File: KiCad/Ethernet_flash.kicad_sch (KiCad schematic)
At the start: 45 parts, among them IC10 TS3DV642A0RUAR, IC11 LSF0204GU12, IC8 TFP410PAP, IC9 MX25UM25645GXDI00-T

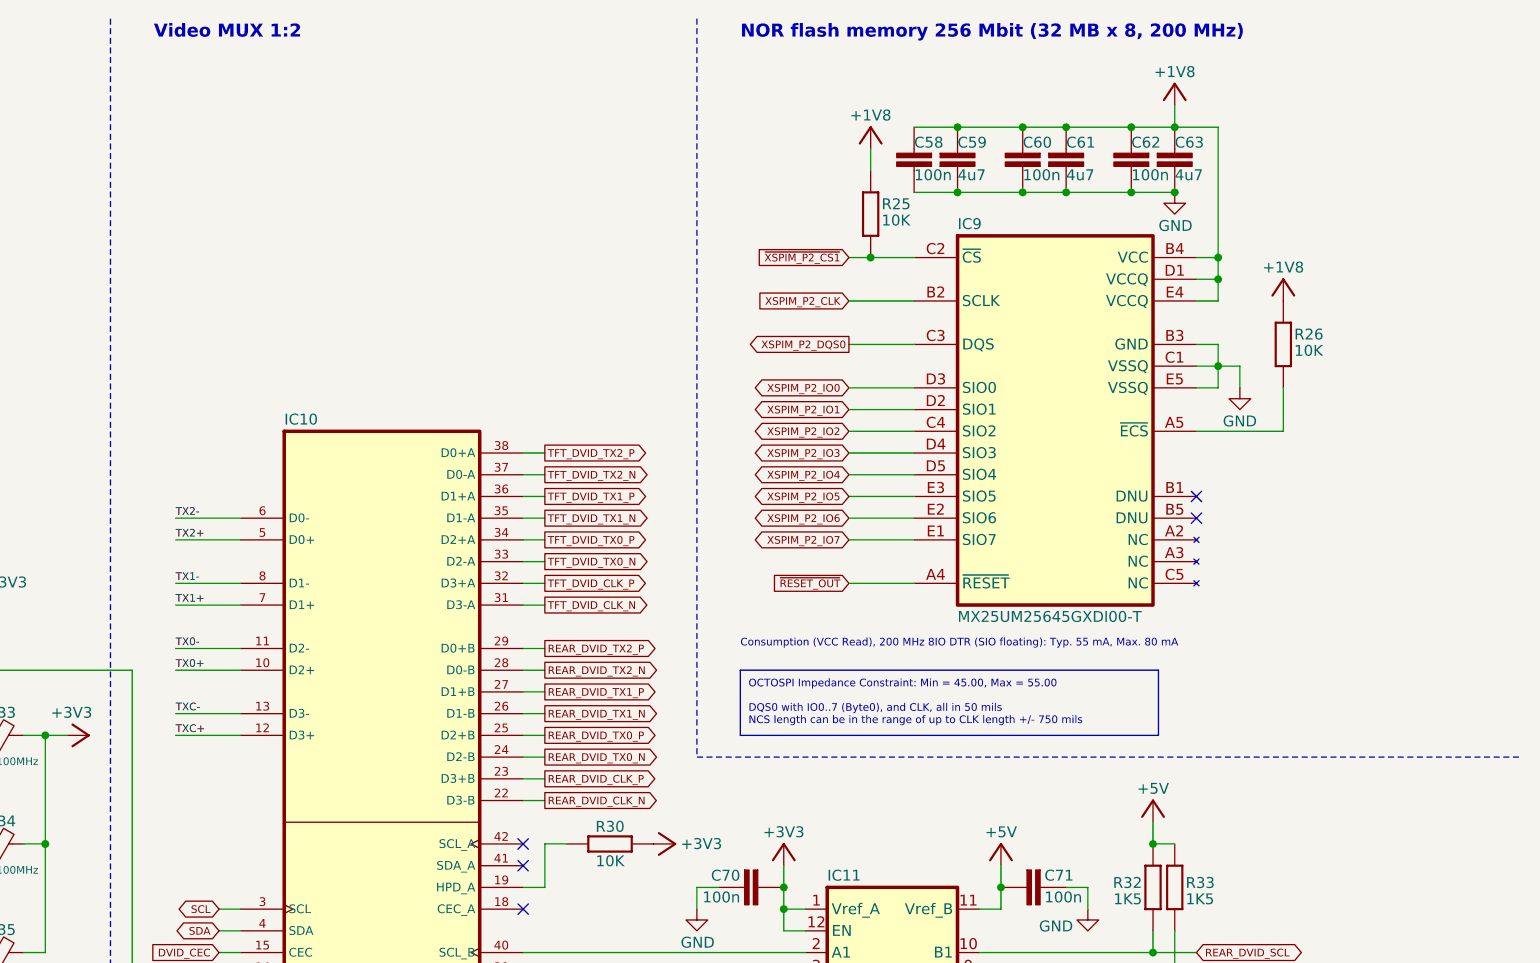
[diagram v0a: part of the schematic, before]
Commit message: USB lanes renamed, OSHWA logo added
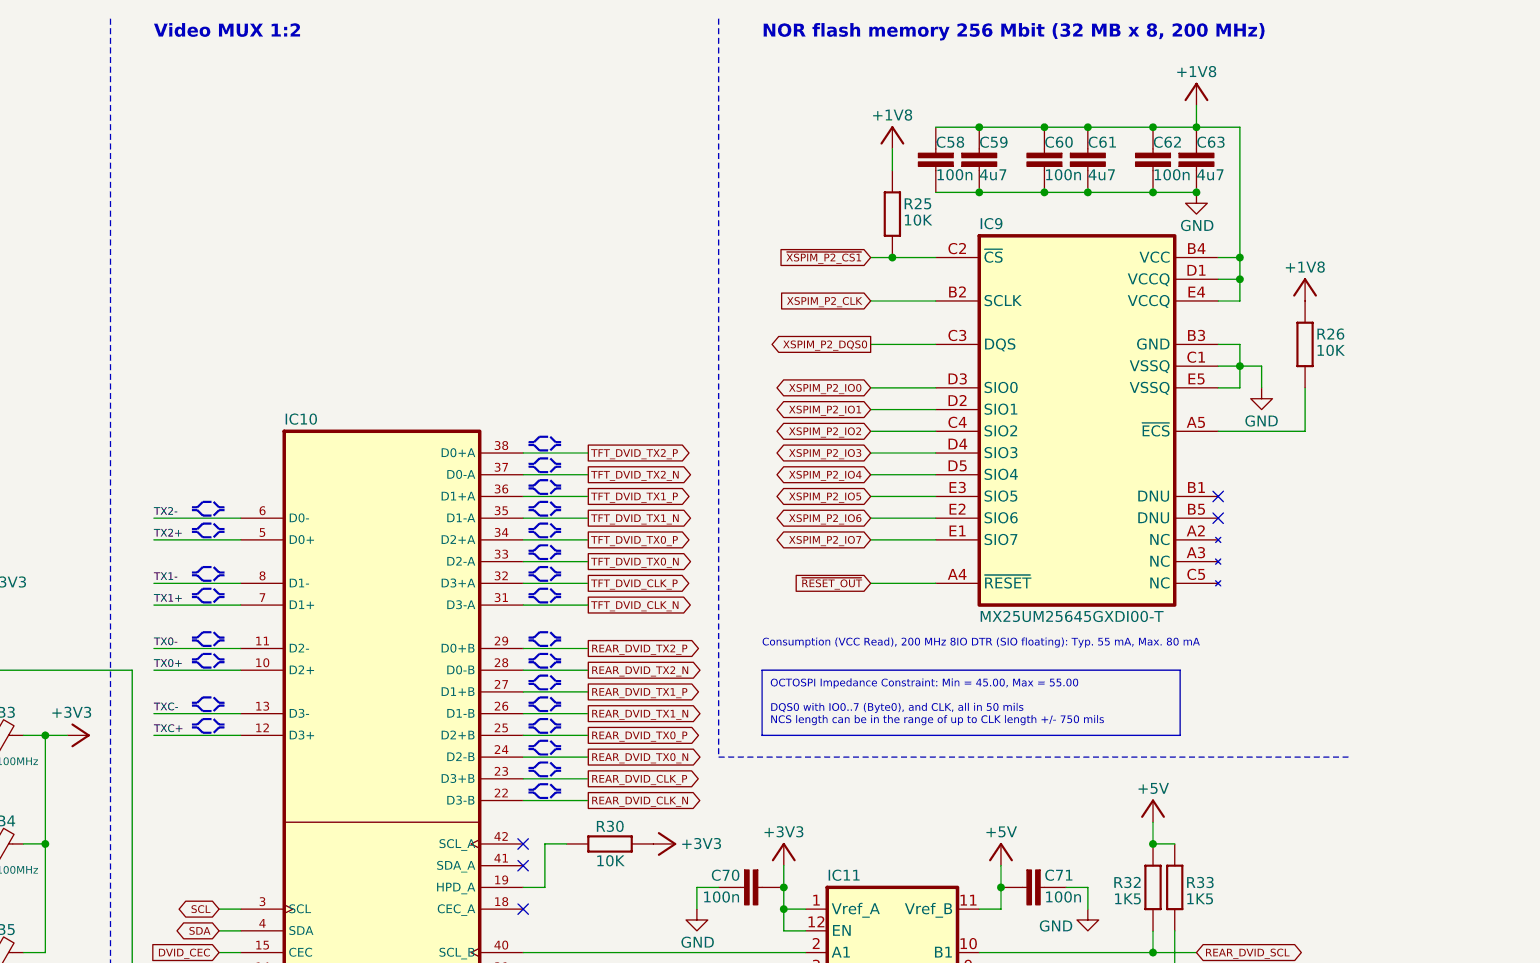
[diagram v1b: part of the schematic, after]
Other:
- moved on the sheet: C58, C59, C60, C61, C62, C63, IC9, R25, R26

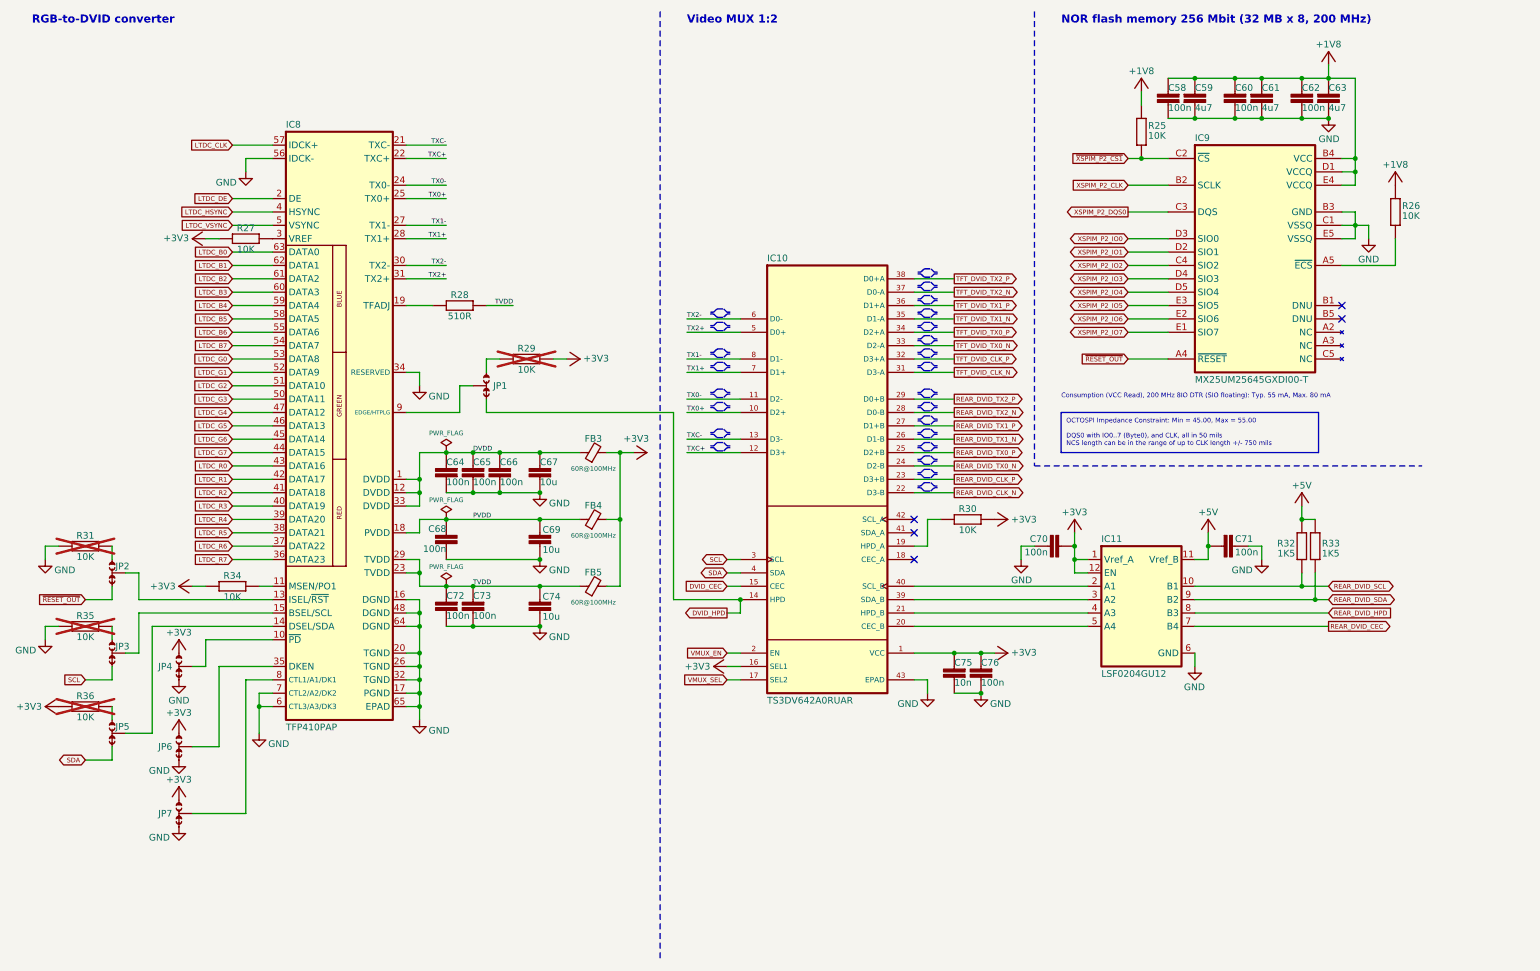
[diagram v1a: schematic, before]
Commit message: Split SoM footprint into two separate 100-pin connectors
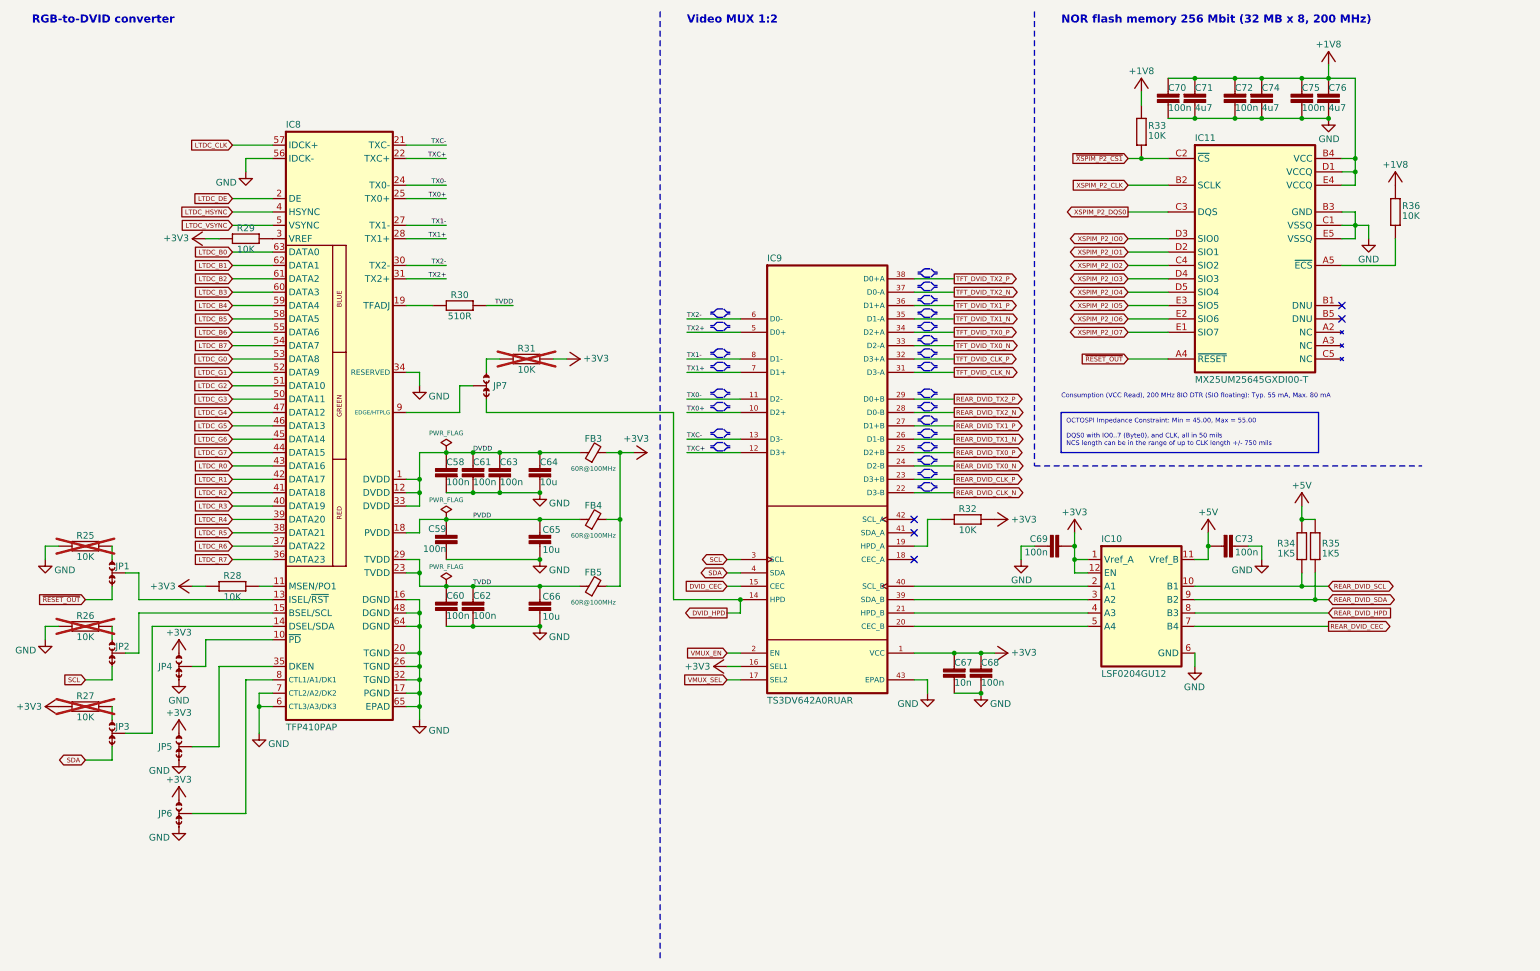
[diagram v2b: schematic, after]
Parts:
- renumbered C64 to C58, C68 to C59, C72 to C60, C65 to C61, C73 to C62, C66 to C63, C67 to C64, C69 to C65, C74 to C66, C75 to C67, C76 to C68, C70 to C69, C58 to C70, C59 to C71, C60 to C72, C71 to C73, C61 to C74, C62 to C75, C63 to C76, IC11 to IC10, IC9 to IC11, IC10 to IC9, JP2 to JP1, JP3 to JP2, JP5 to JP3, JP6 to JP5, JP7 to JP6, JP1 to JP7, R31 to R25, R35 to R26, R36 to R27, R34 to R28, R27 to R29, R28 to R30, R29 to R31, R30 to R32, R25 to R33, R32 to R34, R33 to R35, R26 to R36

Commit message: #20
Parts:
- renumbered JP1 to JP2, JP2 to JP3, JP3 to JP4, JP4 to JP5, JP5 to JP6, JP6 to JP7, JP7 to JP8, R25 to R26, R26 to R27, R27 to R28, R28 to R29, R29 to R30, R30 to R31, R31 to R32, R32 to R33, R33 to R34, R34 to R35, R35 to R36, R36 to R37

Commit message: #21
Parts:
- renumbered JP2 to JP3, JP3 to JP4, JP4 to JP5, JP5 to JP6, JP6 to JP7, JP7 to JP8, JP8 to JP9
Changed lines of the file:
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@@
 		(in_pos_files yes)
 		(dnp no)
-		(property "Reference" "JP2"
+		(property "Reference" "JP3"
 			(at 33.655 120.65 0)
 			(show_name no)
@@
 			(project "BB3plus CM5 STM32H7 module"
 				(path "/1a4f0aea-3a69-423f-8790-3103cd0321c4/6c545e17-ca5e-4b04-9dff-4169dbe59c9e"
-					(reference "JP2")
+					(reference "JP3")
 					(unit 1)
 				)
@@
 		(in_pos_files yes)
 		(dnp no)
-		(property "Reference" "JP5"
+		(property "Reference" "JP6"
 			(at 44.45 139.6999 0)
 			(show_name no)
@@
 			(project "BB3plus CM5 STM32H7 module"
 				(path "/1a4f0aea-3a69-423f-8790-3103cd0321c4/6c545e17-ca5e-4b04-9dff-4169dbe59c9e"
-					(reference "JP5")
+					(reference "JP6")
 					(unit 1)
 				)
@@
 		(in_pos_files yes)
 		(dnp no)
-		(property "Reference" "JP8"
+		(property "Reference" "JP9"
 			(at 105.41 86.3599 0)
 			(show_name no)
@@
 			(project "BB3plus CM5 STM32H7 module"
 				(path "/1a4f0aea-3a69-423f-8790-3103cd0321c4/6c545e17-ca5e-4b04-9dff-4169dbe59c9e"
-					(reference "JP8")
+					(reference "JP9")
 					(unit 1)
 				)
@@
 		(in_pos_files yes)
 		(dnp no)
-		(property "Reference" "JP6"
+		(property "Reference" "JP7"
 			(at 44.45 154.9399 0)
 			(show_name no)
@@
 			(project "BB3plus CM5 STM32H7 module"
 				(path "/1a4f0aea-3a69-423f-8790-3103cd0321c4/6c545e17-ca5e-4b04-9dff-4169dbe59c9e"
-					(reference "JP6")
+					(reference "JP7")
 					(unit 1)
 				)
@@
 		(in_pos_files yes)
 		(dnp no)
-		(property "Reference" "JP4"
+		(property "Reference" "JP5"
 			(at 33.655 151.13 0)
 			(show_name no)
@@
 			(project "BB3plus CM5 STM32H7 module"
 				(path "/1a4f0aea-3a69-423f-8790-3103cd0321c4/6c545e17-ca5e-4b04-9dff-4169dbe59c9e"
-					(reference "JP4")
+					(reference "JP5")
 					(unit 1)
 				)
@@
 		(in_pos_files yes)
 		(dnp no)
-		(property "Reference" "JP3"
+		(property "Reference" "JP4"
 			(at 33.655 135.89 0)
 			(show_name no)
@@
 			(project "BB3plus CM5 STM32H7 module"
 				(path "/1a4f0aea-3a69-423f-8790-3103cd0321c4/6c545e17-ca5e-4b04-9dff-4169dbe59c9e"
-					(reference "JP3")
+					(reference "JP4")
 					(unit 1)
 				)
@@
 		(in_pos_files yes)
 		(dnp no)
-		(property "Reference" "JP7"
+		(property "Reference" "JP8"
 			(at 44.45 167.6399 0)
 			(show_name no)
@@
 			(project "BB3plus CM5 STM32H7 module"
 				(path "/1a4f0aea-3a69-423f-8790-3103cd0321c4/6c545e17-ca5e-4b04-9dff-4169dbe59c9e"
-					(reference "JP7")
+					(reference "JP8")
 					(unit 1)
 				)
